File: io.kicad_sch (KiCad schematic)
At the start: 9 parts, among them SW1 SW_DIP_x08, U12 8255A, U13 SN74HCT138N, U23 8259A

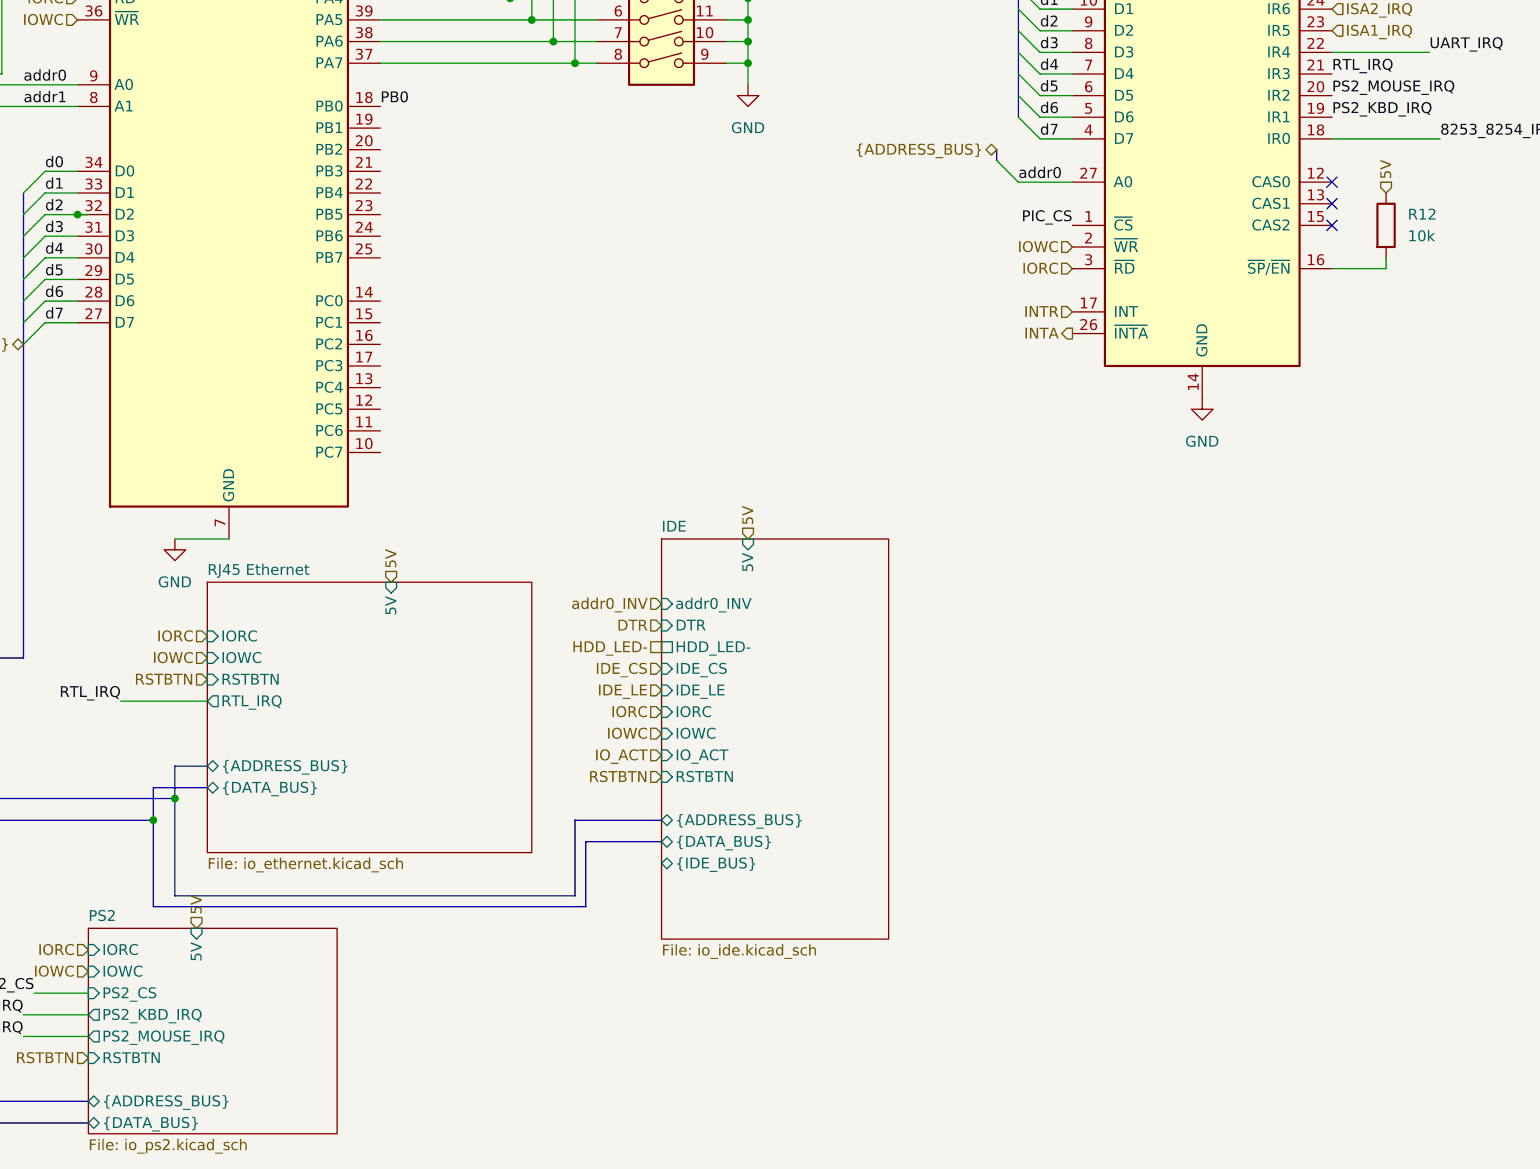
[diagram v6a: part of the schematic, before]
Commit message: ISA card slots, schematic cleanup
Signed-off-by: Lucy Mielke <user@domain.tld>
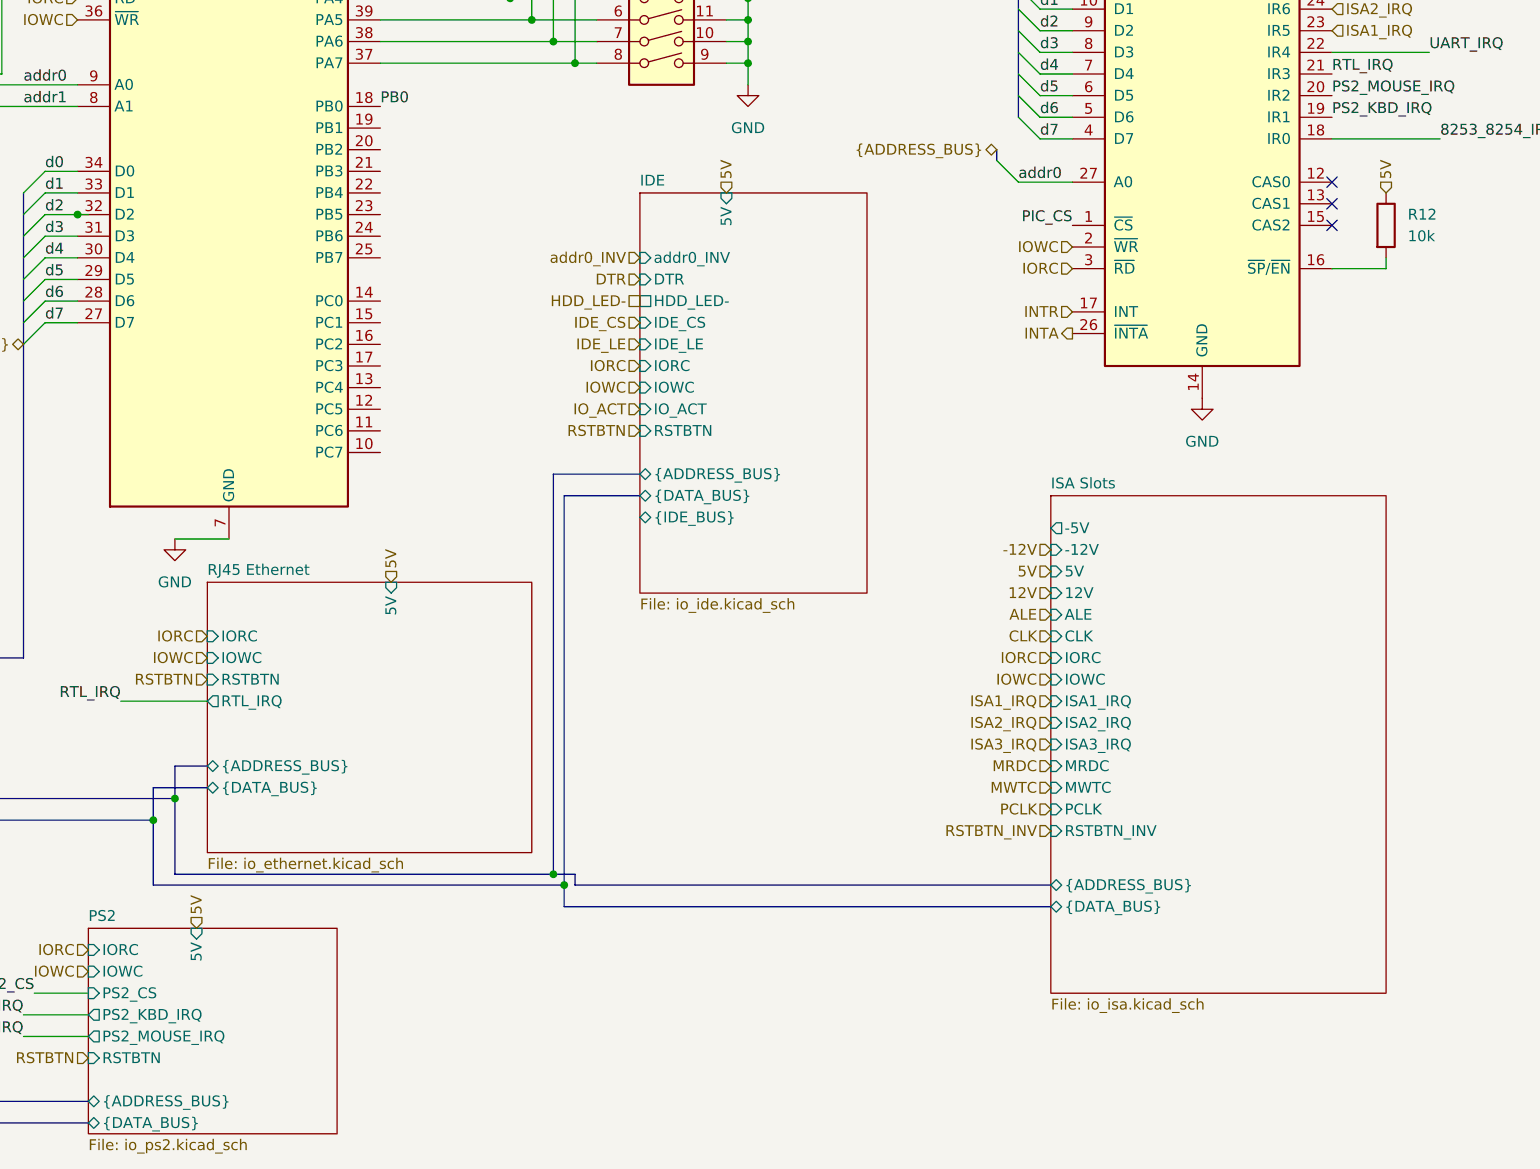
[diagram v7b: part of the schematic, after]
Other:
- added sheet ISA Slots (io_isa.kicad_sch)

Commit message: Fix ERC errors
Signed-off-by: Lucy Mielke <user@domain.tld>
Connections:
- no-connect marks 6 -> 26
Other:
- sheet IDE ports: added IDE_D[0..15], addr[0..19], d[0..7]; removed {ADDRESS_BUS}, {DATA_BUS}, {IDE_BUS}
- sheet ISA Slots ports: added addr[0..19], d[0..7]; removed {ADDRESS_BUS}, {DATA_BUS}
- sheet PS2 ports: added addr[0..19], d[0..7]; removed {ADDRESS_BUS}, {DATA_BUS}
- sheet Programmable Interrupt Timer ports: added addr[0..19], d[0..7]; removed {ADDRESS_BUS}, {DATA_BUS}
- sheet RJ45 Ethernet ports: added addr[0..19], d[0..7]; removed {ADDRESS_BUS}, {DATA_BUS}
- sheet RS232 UART ports: added addr[0..19], d[0..7]; removed {ADDRESS_BUS}, {DATA_BUS}
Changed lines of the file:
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@@
 	)
 	(junction
-		(at 104.14 72.39)
-		(diameter 0)
-		(color 0 0 0 0)
-	)
-	(junction
 		(at 162.56 54.61)
 		(diameter 0)
@@
 	)
 	(no_connect
+		(at 218.44 109.22)
+	)
+	(no_connect
+		(at 139.7 97.79)
+	)
+	(no_connect
+		(at 139.7 72.39)
+	)
+	(no_connect
+		(at 139.7 62.23)
+	)
+	(no_connect
+		(at 139.7 82.55)
+	)
+	(no_connect
 		(at 69.85 63.5)
 	)
 	(no_connect
+		(at 139.7 64.77)
+	)
+	(no_connect
+		(at 139.7 74.93)
+	)
+	(no_connect
 		(at 251.46 73.66)
 	)
 	(no_connect
+		(at 139.7 85.09)
+	)
+	(no_connect
 		(at 69.85 60.96)
 	)
 	(no_connect
+		(at 139.7 69.85)
+	)
+	(no_connect
 		(at 69.85 66.04)
 	)
 	(no_connect
+		(at 54.61 167.64)
+	)
+	(no_connect
+		(at 139.7 92.71)
+	)
+	(no_connect
+		(at 139.7 67.31)
+	)
+	(no_connect
 		(at 251.46 68.58)
 	)
@@
 		(at 251.46 71.12)
 	)
+	(no_connect
+		(at 170.18 107.95)
+	)
+	(no_connect
+		(at 139.7 77.47)
+	)
+	(no_connect
+		(at 76.2 48.26)
+	)
+	(no_connect
+		(at 54.61 172.72)
+	)
+	(no_connect
+		(at 139.7 87.63)
+	)
+	(no_connect
+		(at 139.7 95.25)
+	)
+	(no_connect
+		(at 139.7 100.33)
+	)
+	(no_connect
+		(at 139.7 90.17)
+	)
 	(bus_entry
 		(at 100.33 67.31)
@@
 	(wire
 		(pts
-			(xy 104.14 72.39) (xy 105.41 72.39)
-		)
-		(stroke
-			(width 0)
-			(type default)
-		)
-	)
-	(wire
-		(pts
 			(xy 72.39 43.18) (xy 72.39 36.83)
 		)
@@
 		)
 	)
-	(hierarchical_label "{DATA_BUS}"
+	(hierarchical_label "d[0..7]"
 		(shape bidirectional)
 		(at 97.79 87.63 180)
@@
 		)
 	)
-	(hierarchical_label "{DATA_BUS}"
+	(hierarchical_label "d[0..7]"
 		(shape bidirectional)
 		(at 214.63 34.29 180)
@@
 		)
 	)
-	(hierarchical_label "{ADDRESS_BUS}"
+	(hierarchical_label "addr[0..19]"
 		(shape bidirectional)
 		(at 13.97 85.09 270)
@@
 		)
 	)
-	(hierarchical_label "{ADDRESS_BUS}"
+	(hierarchical_label "addr[0..19]"
 		(shape bidirectional)
 		(at 212.09 64.77 180)
@@
 			)
 		)
-		(pin "{ADDRESS_BUS}" bidirectional
+		(pin "addr[0..19]" bidirectional
 			(at 105.41 176.53 180)
 			(effects
@@
 			)
 		)
-		(pin "{DATA_BUS}" bidirectional
+		(pin "d[0..7]" bidirectional
 			(at 105.41 179.07 180)
 			(effects
@@
 			)
 		)
-		(pin "{ADDRESS_BUS}" bidirectional
+		(pin "addr[0..19]" bidirectional
 			(at 54.61 181.61 0)
 			(effects
@@
 			)
 		)
-		(pin "{DATA_BUS}" bidirectional
+		(pin "d[0..7]" bidirectional
 			(at 54.61 184.15 0)
 			(effects
@@
 			)
 		)
-		(pin "{ADDRESS_BUS}" bidirectional
+		(pin "addr[0..19]" bidirectional
 			(at 170.18 102.87 180)
 			(effects
@@
 			)
 		)
-		(pin "{DATA_BUS}" bidirectional
+		(pin "d[0..7]" bidirectional
 			(at 170.18 105.41 180)
 			(effects
@@
 			)
 		)
-		(pin "{IDE_BUS}" bidirectional
+		(pin "IDE_D[0..15]" bidirectional
 			(at 170.18 107.95 180)
 			(effects
@@
 			)
 		)
-		(pin "{ADDRESS_BUS}" bidirectional
+		(pin "addr[0..19]" bidirectional
 			(at 40.64 121.92 0)
 			(effects
@@
 			)
 		)
-		(pin "{DATA_BUS}" bidirectional
+		(pin "d[0..7]" bidirectional
 			(at 40.64 124.46 0)
 			(effects
@@
 			)
 		)
-		(pin "{ADDRESS_BUS}" bidirectional
+		(pin "addr[0..19]" bidirectional
 			(at 218.44 151.13 180)
 			(effects
@@
 			)
 		)
-		(pin "{DATA_BUS}" bidirectional
+		(pin "d[0..7]" bidirectional
 			(at 218.44 153.67 180)
 			(effects
@@
 			)
 		)
-		(pin "{ADDRESS_BUS}" bidirectional
+		(pin "addr[0..19]" bidirectional
 			(at 119.38 137.16 180)
 			(effects
@@
 			)
 		)
-		(pin "{DATA_BUS}" bidirectional
+		(pin "d[0..7]" bidirectional
 			(at 119.38 139.7 180)
 			(effects
